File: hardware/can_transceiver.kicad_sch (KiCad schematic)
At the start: 10 parts

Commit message: Add the Cube project
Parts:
- removed D?: PESD2CAN.215, Package_TO_SOT_SMD:SOT-23, symbol Local_Library:D_TVS_x2_AAC-Device
- removed J?: Terminator, Connector_PinHeader_2.54mm:PinHeader_1x02_P2.54mm_Vertical, symbol Local_Library:Jumper_NO_Small-Device
- removed R?: 120R, Resistor_SMD:R_0402_1005Metric, symbol Device:R_Small
- added D2: PESD2CAN.215, Package_TO_SOT_SMD:SOT-23, symbol Device:D_TVS_Dual_AAC
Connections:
- net CAN+: now also D2.1 (A1)
- net CAN-: now also D2.2 (A2)
- net GND: now also D2.3 (common)
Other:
- moved on the sheet: C?, FB?, TP?

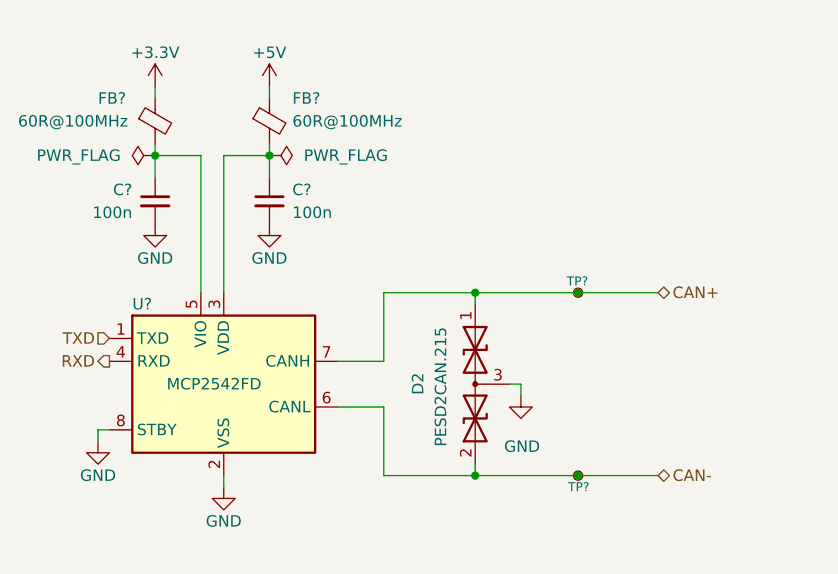
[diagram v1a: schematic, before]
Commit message: Improve the schematic
- add anti-aliasing filters
- rearrange the main connector signals
- improve the power filtering
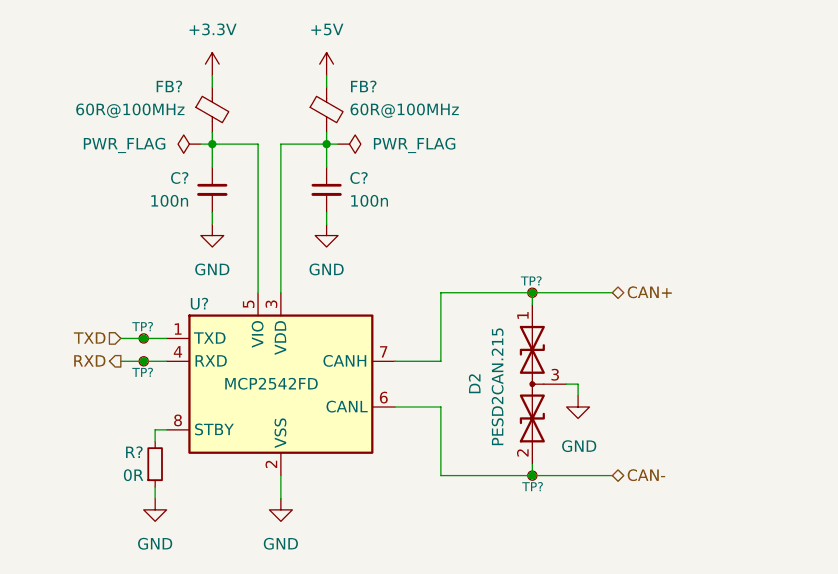
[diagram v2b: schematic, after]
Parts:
- added R?: 0R, Resistor_SMD:R_0603_1608Metric, symbol Device:R_Small
- added TP? (x2): TestPoint_Small, TestPoint:TestPoint_Pad_D1.0mm, symbol Connector:TestPoint_Small
- C? (x2): footprint Capacitor_SMD:C_0402_1005Metric_Pad0.74x0.62mm_HandSolder -> Capacitor_SMD:C_0603_1608Metric
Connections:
- net GND: now also R?.1; no longer U?.8 (STBY)
- net RXD: now also TP?.1
- net TXD: now also TP?.1
- new net: R?.2, U?.8 (STBY)
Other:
- moved on the sheet: C?, D2, FB?, TP?, U?

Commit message: Set component values
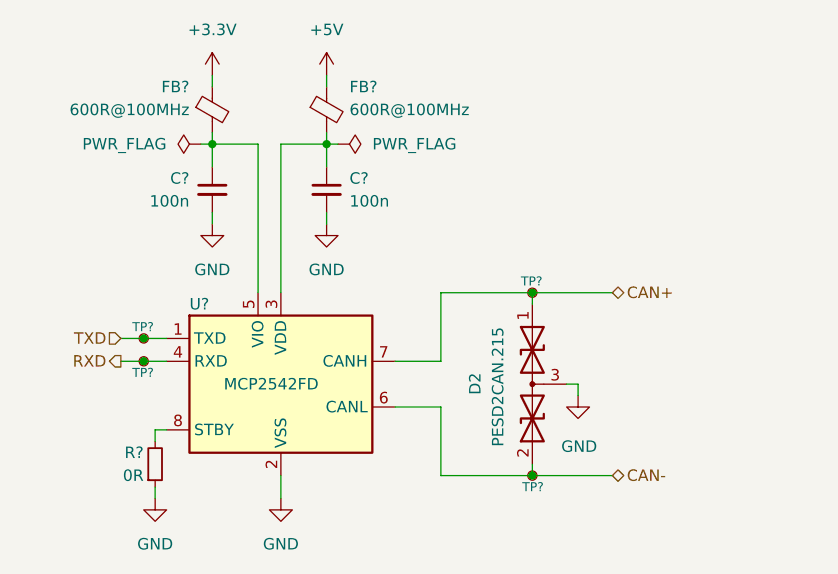
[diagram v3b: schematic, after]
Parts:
- FB? (x2): value 60R@100MHz -> 600R@100MHz
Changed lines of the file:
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@@
       (effects (font (size 1.27 1.27)) (justify left))
     )
-    (property "Value" "60R@100MHz" (at 148.59 77.47 0)
+    (property "Value" "600R@100MHz" (at 148.59 77.47 0)
       (effects (font (size 1.27 1.27)) (justify left))
     )
@@
   (symbol (lib_id "Device:FerriteBead_Small") (at 133.35 77.47 0) (unit 1)
     (in_bom yes) (on_board yes) (dnp no)
-    (property "Reference" "FB?" (at 127 74.93 0)
-      (effects (font (size 1.27 1.27)) (justify left))
-    )
-    (property "Value" "60R@100MHz" (at 118.11 77.47 0)
-      (effects (font (size 1.27 1.27)) (justify left))
+    (property "Reference" "FB?" (at 130.81 74.93 0)
+      (effects (font (size 1.27 1.27)) (justify right))
+    )
+    (property "Value" "600R@100MHz" (at 130.81 77.47 0)
+      (effects (font (size 1.27 1.27)) (justify right))
     )
     (property "Footprint" "Inductor_SMD:L_0603_1608Metric" (at 131.572 77.47 90)
@@
         )
         (path "/b652b05a-4e3d-4ad1-b032-18886abe7d45/38408e41-dfb1-4c27-acb0-3f1224cc8789/f1ed15a3-9302-436f-b25a-713477aeadf3"
-          (reference "R35") (unit 1)
-        )
-        (path "/b652b05a-4e3d-4ad1-b032-18886abe7d45/38408e41-dfb1-4c27-acb0-3f1224cc8789/eec2c93a-0fce-4d3a-ab43-9e1e0481c06c"
           (reference "R36") (unit 1)
         )
-      )
+        (path "/b652b05a-4e3d-4ad1-b032-18886abe7d45/38408e41-dfb1-4c27-acb0-3f1224cc8789/eec2c93a-0fce-4d3a-ab43-9e1e0481c06c"
+          (reference "R37") (unit 1)
+        )
+      )

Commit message: Improve the schematic according to the feedback
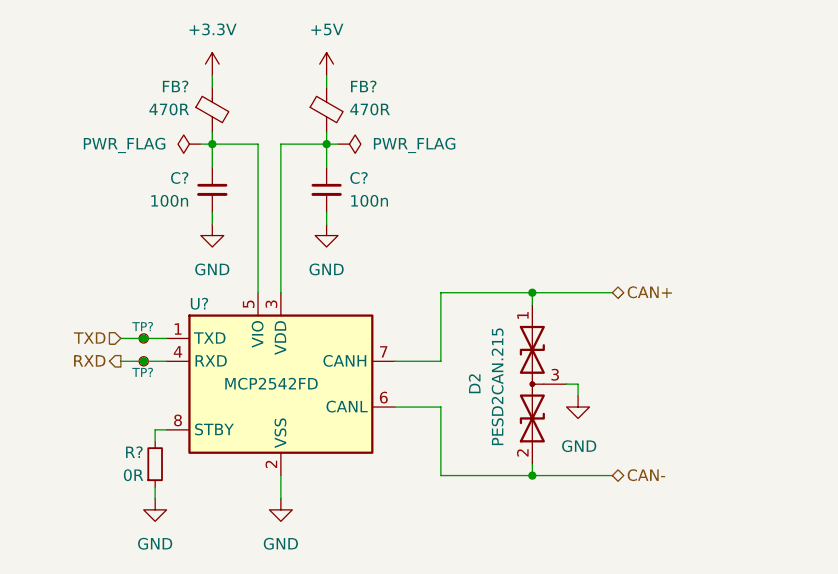
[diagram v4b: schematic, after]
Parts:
- removed TP? (x2): TestPoint_Small, TestPoint:TestPoint_Pad_D1.0mm, symbol Connector:TestPoint_Small
- FB? (x2): value 600R@100MHz -> 470R

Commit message: Improve the diagram based on the feedback
- add an input LC filter
- remove the USB connector
- add a programmer connector
- move optocouplers into a subsheet
- add a suspension tension meter IC
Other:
- title: (none) -> CAN Transceiver
